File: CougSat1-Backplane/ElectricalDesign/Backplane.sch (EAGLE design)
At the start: 16 parts, among them J1 COUGSATBUSBACKPLANE, J2 COUGSATBUSBACKPLANE, J3 COUGSATBUSBACKPLANE, J4 COUGSATBUSBACKPLANE, J5 COUGSATBUSBACKPLANE, J6 COUGSATBUSBACKPLANE, J7 COUGSATBUSBACKPLANE, J8 COUGSATBUSBACKPLANE

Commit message: Updated Backplane Schematic
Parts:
- removed H3, H4: MOUNTING_HOLE_PLAIN3MMBOLT, CougsInSpace:MOUNTING_HOLE_PLAIN3MMBOLT
- removed IMG1: COUGSINSPACELOGOSMALL, CougsInSpace:COUGSINSPACELOGOSMALL
- removed IMG2: COUGSINSPACELOGOTEXT, CougsInSpace:COUGSINSPACELOGOTEXT
- removed IMG3: SIGNATUREHENDRIK, CougsInSpace:SIGNATUREHENDRIK
- removed IMG4: SIGNATUREHENDRIK-HAM, CougsInSpace:SIGNATUREHENDRIK-HAM
- added C1, C2: 100nF 10%, CougsInSpace-Capacitors:CAP-V-100NF-1608
- added J10, J9: Deployment Switch, CougsInSpace-Connectors:1X04-PICOLOCK
- added R1, R2: 0Ω <20mΩ, CougsInSpace-Resistors:RES-V-0-1608
- H1, H2: value MOUNTING_HOLE_PLAIN3MMBOLT -> M3; device CougsInSpace:MOUNTING_HOLE_PLAIN3MMBOLT -> CougsInSpace-Hardware:MOUNTING_HOLE-3.3
- J1, J2, J3, J4, J5, J6, J7, J8: value COUGSATBUSBACKPLANE -> CougSat Socket; device CougsInSpace:COUGSATBUSBACKPLANE -> CougsInSpace-Connectors:CIS_CARD-SODIMM-DDR1
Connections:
- removed net COM_IRQ: J1RCS.COM_IRQ, J2RCS.COM_IRQ, J3RCS.COM_IRQ, J4RCS.COM_IRQ, J5RCS.COM_IRQ, J6RCS.COM_IRQ, J7RCS.COM_IRQ, J8RCS.COM_IRQ
- removed net COM_USART_CLK: J1RCS.COM_USART_CLK, J2RCS.COM_USART_CLK, J3RCS.COM_USART_CLK, J4RCS.COM_USART_CLK, J5RCS.COM_USART_CLK, J6RCS.COM_USART_CLK, J7RCS.COM_USART_CLK, J8RCS.COM_USART_CLK
- removed net COM_USART_RX: J1RCS.COM_USART_RX, J2RCS.COM_USART_RX, J3RCS.COM_USART_RX, J4RCS.COM_USART_RX, J5RCS.COM_USART_RX, J6RCS.COM_USART_RX, J7RCS.COM_USART_RX, J8RCS.COM_USART_RX
- removed net COM_USART_TX: J1RCS.COM_USART_TX, J2RCS.COM_USART_TX, J3RCS.COM_USART_TX, J4RCS.COM_USART_TX, J5RCS.COM_USART_TX, J6RCS.COM_USART_TX, J7RCS.COM_USART_TX, J8RCS.COM_USART_TX
- removed net CTRL_RESET: J1DATABUS.CTRL_!RESET, J2DATABUS.CTRL_!RESET, J3DATABUS.CTRL_!RESET, J4DATABUS.CTRL_!RESET, J5DATABUS.CTRL_!RESET, J6DATABUS.CTRL_!RESET, J7DATABUS.CTRL_!RESET, J8DATABUS.CTRL_!RESET
- removed net GPIO_153: J1GPIO.GPIO_153, J2GPIO.GPIO_153, J3GPIO.GPIO_153, J4GPIO.GPIO_153, J5GPIO.GPIO_153, J6GPIO.GPIO_153, J7GPIO.GPIO_153, J8GPIO.GPIO_153
- removed net GPIO_155: J1GPIO.GPIO_155, J2GPIO.GPIO_155, J3GPIO.GPIO_155, J4GPIO.GPIO_155, J5GPIO.GPIO_155, J6GPIO.GPIO_155, J7GPIO.GPIO_155, J8GPIO.GPIO_155
- removed net GPIO_157: J1GPIO.GPIO_157, J2GPIO.GPIO_157, J3GPIO.GPIO_157, J4GPIO.GPIO_157, J5GPIO.GPIO_157, J6GPIO.GPIO_157, J7GPIO.GPIO_157, J8GPIO.GPIO_157
- removed net GPIO_158: J1GPIO.GPIO_158, J2GPIO.GPIO_158, J3GPIO.GPIO_158, J4GPIO.GPIO_158, J5GPIO.GPIO_158, J6GPIO.GPIO_158, J7GPIO.GPIO_158, J8GPIO.GPIO_158
- removed net GPIO_159: J1GPIO.GPIO_159, J2GPIO.GPIO_159, J3GPIO.GPIO_159, J4GPIO.GPIO_159, J5GPIO.GPIO_159, J6GPIO.GPIO_159, J7GPIO.GPIO_159, J8GPIO.GPIO_159
- removed net GPIO_161: J1GPIO.GPIO_161, J2GPIO.GPIO_161, J3GPIO.GPIO_161, J4GPIO.GPIO_161, J5GPIO.GPIO_161, J6GPIO.GPIO_161, J7GPIO.GPIO_161, J8GPIO.GPIO_161
- removed net GPIO_163: J1GPIO.GPIO_163, J2GPIO.GPIO_163, J3GPIO.GPIO_163, J4GPIO.GPIO_163, J5GPIO.GPIO_163, J6GPIO.GPIO_163, J7GPIO.GPIO_163, J8GPIO.GPIO_163
- removed net GPIO_165: J1GPIO.GPIO_165, J2GPIO.GPIO_165, J3GPIO.GPIO_165, J4GPIO.GPIO_165, J5GPIO.GPIO_165, J6GPIO.GPIO_165, J7GPIO.GPIO_165, J8GPIO.GPIO_165
- removed net GPIO_167: J1GPIO.GPIO_167, J2GPIO.GPIO_167, J3GPIO.GPIO_167, J4GPIO.GPIO_167, J5GPIO.GPIO_167, J6GPIO.GPIO_167, J7GPIO.GPIO_167, J8GPIO.GPIO_167
- removed net PMIC_I2C_SCL: J1DATABUS.PMIC_I2C_SCL, J2DATABUS.PMIC_I2C_SCL, J3DATABUS.PMIC_I2C_SCL, J4DATABUS.PMIC_I2C_SCL, J5DATABUS.PMIC_I2C_SCL, J6DATABUS.PMIC_I2C_SCL, J7DATABUS.PMIC_I2C_SCL, J8DATABUS.PMIC_I2C_SCL
- removed net PMIC_I2C_SDA: J1DATABUS.PMIC_I2C_SDA, J2DATABUS.PMIC_I2C_SDA, J3DATABUS.PMIC_I2C_SDA, J4DATABUS.PMIC_I2C_SDA, J5DATABUS.PMIC_I2C_SDA, J6DATABUS.PMIC_I2C_SDA, J7DATABUS.PMIC_I2C_SDA, J8DATABUS.PMIC_I2C_SDA
- removed net PWR_CTRL_UMB: J1POWER.PWR_CTRL_UMB, J2POWER.PWR_CTRL_UMB, J3POWER.PWR_CTRL_UMB, J4POWER.PWR_CTRL_UMB, J5POWER.PWR_CTRL_UMB, J6POWER.PWR_CTRL_UMB, J7POWER.PWR_CTRL_UMB, J8POWER.PWR_CTRL_UMB
- removed net SUP_3V3_0: J1POWER.SUP_3V3_0, J2POWER.SUP_3V3_0, J3POWER.SUP_3V3_0, J4POWER.SUP_3V3_0, J5POWER.SUP_3V3_0, J6POWER.SUP_3V3_0, J7POWER.SUP_3V3_0, J8POWER.SUP_3V3_0
- removed net SUP_3V3_1: J1POWER.SUP_3V3_1, J2POWER.SUP_3V3_1, J3POWER.SUP_3V3_1, J4POWER.SUP_3V3_1, J5POWER.SUP_3V3_1, J6POWER.SUP_3V3_1, J7POWER.SUP_3V3_1, J8POWER.SUP_3V3_1
- removed net SUP_3V3_2: J1POWER.SUP_3V3_2, J2POWER.SUP_3V3_2, J3POWER.SUP_3V3_2, J4POWER.SUP_3V3_2, J5POWER.SUP_3V3_2, J6POWER.SUP_3V3_2, J7POWER.SUP_3V3_2, J8POWER.SUP_3V3_2
- removed net SUP_3V3_3: J1POWER.SUP_3V3_3, J2POWER.SUP_3V3_3, J3POWER.SUP_3V3_3, J4POWER.SUP_3V3_3, J5POWER.SUP_3V3_3, J6POWER.SUP_3V3_3, J7POWER.SUP_3V3_3, J8POWER.SUP_3V3_3
- removed net SUP_3V3_4: J1POWER.SUP_3V3_4, J2POWER.SUP_3V3_4, J3POWER.SUP_3V3_4, J4POWER.SUP_3V3_4, J5POWER.SUP_3V3_4, J6POWER.SUP_3V3_4, J7POWER.SUP_3V3_4, J8POWER.SUP_3V3_4
- removed net SUP_3V3_5: J1POWER.SUP_3V3_5, J2POWER.SUP_3V3_5, J3POWER.SUP_3V3_5, J4POWER.SUP_3V3_5, J5POWER.SUP_3V3_5, J6POWER.SUP_3V3_5, J7POWER.SUP_3V3_5, J8POWER.SUP_3V3_5
- removed net SUP_5V0_0: J1POWER.SUP_5V0_0, J2POWER.SUP_5V0_0, J3POWER.SUP_5V0_0, J4POWER.SUP_5V0_0, J5POWER.SUP_5V0_0, J6POWER.SUP_5V0_0, J7POWER.SUP_5V0_0, J8POWER.SUP_5V0_0
- removed net SUP_5V0_1: J1POWER.SUP_5V0_1, J2POWER.SUP_5V0_1, J3POWER.SUP_5V0_1, J4POWER.SUP_5V0_1, J5POWER.SUP_5V0_1, J6POWER.SUP_5V0_1, J7POWER.SUP_5V0_1, J8POWER.SUP_5V0_1
- removed net SUP_5VIN: J1POWER.SUP_5VIN, J2POWER.SUP_5VIN, J3POWER.SUP_5VIN, J4POWER.SUP_5VIN, J5POWER.SUP_5VIN, J6POWER.SUP_5VIN, J7POWER.SUP_5VIN, J8POWER.SUP_5VIN
- removed net SUP_UNREG_0: J1POWER.SUP_UNREG_0, J2POWER.SUP_UNREG_0, J3POWER.SUP_UNREG_0, J4POWER.SUP_UNREG_0, J5POWER.SUP_UNREG_0, J6POWER.SUP_UNREG_0, J7POWER.SUP_UNREG_0, J8POWER.SUP_UNREG_0
- removed net SUP_UNREG_1: J1POWER.SUP_UNREG_1, J2POWER.SUP_UNREG_1, J3POWER.SUP_UNREG_1, J4POWER.SUP_UNREG_1, J5POWER.SUP_UNREG_1, J6POWER.SUP_UNREG_1, J7POWER.SUP_UNREG_1, J8POWER.SUP_UNREG_1
- new net BUS_JTAG_EN-0: J1JTAG.BUS_JTAG_EN-0, J2JTAG.BUS_JTAG_EN-0, J3JTAG.BUS_JTAG_EN-0, J4JTAG.BUS_JTAG_EN-0, J5JTAG.BUS_JTAG_EN-0, J6JTAG.BUS_JTAG_EN-0, J7JTAG.BUS_JTAG_EN-0, J8JTAG.BUS_JTAG_EN-0
- new net BUS_JTAG_EN-1: J1JTAG.BUS_JTAG_EN-1, J2JTAG.BUS_JTAG_EN-1, J3JTAG.BUS_JTAG_EN-1, J4JTAG.BUS_JTAG_EN-1, J5JTAG.BUS_JTAG_EN-1, J6JTAG.BUS_JTAG_EN-1, J7JTAG.BUS_JTAG_EN-1, J8JTAG.BUS_JTAG_EN-1
- new net BUS_JTAG_EN-2: J1JTAG.BUS_JTAG_EN-2, J2JTAG.BUS_JTAG_EN-2, J3JTAG.BUS_JTAG_EN-2, J4JTAG.BUS_JTAG_EN-2, J5JTAG.BUS_JTAG_EN-2, J6JTAG.BUS_JTAG_EN-2, J7JTAG.BUS_JTAG_EN-2, J8JTAG.BUS_JTAG_EN-2
- new net BUS_JTAG_EN-3: J1JTAG.BUS_JTAG_EN-3, J2JTAG.BUS_JTAG_EN-3, J3JTAG.BUS_JTAG_EN-3, J4JTAG.BUS_JTAG_EN-3, J5JTAG.BUS_JTAG_EN-3, J6JTAG.BUS_JTAG_EN-3, J7JTAG.BUS_JTAG_EN-3, J8JTAG.BUS_JTAG_EN-3
- new net CHASSIS: C1.1, C2.1, H1.MOUNT, H2.MOUNT, R1.2, R2.2
- new net COM_SPI_CS: J1DATA.COM_SPI_CS, J2DATA.COM_SPI_CS, J3DATA.COM_SPI_CS, J4DATA.COM_SPI_CS, J5DATA.COM_SPI_CS, J6DATA.COM_SPI_CS, J7DATA.COM_SPI_CS, J8DATA.COM_SPI_CS
- new net COM_SPI_MISO: J1DATA.COM_SPI_MISO, J2DATA.COM_SPI_MISO, J3DATA.COM_SPI_MISO, J4DATA.COM_SPI_MISO, J5DATA.COM_SPI_MISO, J6DATA.COM_SPI_MISO, J7DATA.COM_SPI_MISO, J8DATA.COM_SPI_MISO
- new net COM_SPI_MOSI: J1DATA.COM_SPI_MOSI, J2DATA.COM_SPI_MOSI, J3DATA.COM_SPI_MOSI, J4DATA.COM_SPI_MOSI, J5DATA.COM_SPI_MOSI, J6DATA.COM_SPI_MOSI, J7DATA.COM_SPI_MOSI, J8DATA.COM_SPI_MOSI
- new net COM_SPI_SCK: J1DATA.COM_SPI_SCK, J2DATA.COM_SPI_SCK, J3DATA.COM_SPI_SCK, J4DATA.COM_SPI_SCK, J5DATA.COM_SPI_SCK, J6DATA.COM_SPI_SCK, J7DATA.COM_SPI_SCK, J8DATA.COM_SPI_SCK
- new net CTRL_!RESET: J1DATA.CTRL_!RESET, J2DATA.CTRL_!RESET, J3DATA.CTRL_!RESET, J4DATA.CTRL_!RESET, J5DATA.CTRL_!RESET, J6DATA.CTRL_!RESET, J7DATA.CTRL_!RESET, J8DATA.CTRL_!RESET
- new net GPIO-0: J1GPIO.GPIO-0, J2GPIO.GPIO-0, J3GPIO.GPIO-0, J4GPIO.GPIO-0, J5GPIO.GPIO-0, J6GPIO.GPIO-0, J7GPIO.GPIO-0, J8GPIO.GPIO-0
- new net GPIO-1: J1GPIO.GPIO-1, J2GPIO.GPIO-1, J3GPIO.GPIO-1, J4GPIO.GPIO-1, J5GPIO.GPIO-1, J6GPIO.GPIO-1, J7GPIO.GPIO-1, J8GPIO.GPIO-1
- new net GPIO-2: J1GPIO.GPIO-2, J2GPIO.GPIO-2, J3GPIO.GPIO-2, J4GPIO.GPIO-2, J5GPIO.GPIO-2, J6GPIO.GPIO-2, J7GPIO.GPIO-2, J8GPIO.GPIO-2
- new net GPIO-3: J1GPIO.GPIO-3, J2GPIO.GPIO-3, J3GPIO.GPIO-3, J4GPIO.GPIO-3, J5GPIO.GPIO-3, J6GPIO.GPIO-3, J7GPIO.GPIO-3, J8GPIO.GPIO-3
- new net GPIO-4: J1GPIO.GPIO-4, J2GPIO.GPIO-4, J3GPIO.GPIO-4, J4GPIO.GPIO-4, J5GPIO.GPIO-4, J6GPIO.GPIO-4, J7GPIO.GPIO-4, J8GPIO.GPIO-4
- new net GPIO-5: J1GPIO.GPIO-5, J2GPIO.GPIO-5, J3GPIO.GPIO-5, J4GPIO.GPIO-5, J5GPIO.GPIO-5, J6GPIO.GPIO-5, J7GPIO.GPIO-5, J8GPIO.GPIO-5
- new net GPIO-6: J1GPIO.GPIO-6, J2GPIO.GPIO-6, J3GPIO.GPIO-6, J4GPIO.GPIO-6, J5GPIO.GPIO-6, J6GPIO.GPIO-6, J7GPIO.GPIO-6, J8GPIO.GPIO-6
- new net GPIO-7: J1GPIO.GPIO-7, J2GPIO.GPIO-7, J3GPIO.GPIO-7, J4GPIO.GPIO-7, J5GPIO.GPIO-7, J6GPIO.GPIO-7, J7GPIO.GPIO-7, J8GPIO.GPIO-7
- new net GPIO-8: J1GPIO.GPIO-8, J2GPIO.GPIO-8, J3GPIO.GPIO-8, J4GPIO.GPIO-8, J5GPIO.GPIO-8, J6GPIO.GPIO-8, J7GPIO.GPIO-8, J8GPIO.GPIO-8
- new net GPIO-9: J1GPIO.GPIO-9, J2GPIO.GPIO-9, J3GPIO.GPIO-9, J4GPIO.GPIO-9, J5GPIO.GPIO-9, J6GPIO.GPIO-9, J7GPIO.GPIO-9, J8GPIO.GPIO-9
- new net PR_3.3V-0: J1POWER.PR_3.3V-0, J2POWER.PR_3.3V-0, J3POWER.PR_3.3V-0, J4POWER.PR_3.3V-0, J5POWER.PR_3.3V-0, J6POWER.PR_3.3V-0, J7POWER.PR_3.3V-0, J8POWER.PR_3.3V-0
- new net PR_3.3V-1: J1POWER.PR_3.3V-1, J2POWER.PR_3.3V-1, J3POWER.PR_3.3V-1, J4POWER.PR_3.3V-1, J5POWER.PR_3.3V-1, J6POWER.PR_3.3V-1, J7POWER.PR_3.3V-1, J8POWER.PR_3.3V-1
- new net PR_3.3V-10: J1POWER.PR_3.3V-10, J2POWER.PR_3.3V-10, J3POWER.PR_3.3V-10, J4POWER.PR_3.3V-10, J5POWER.PR_3.3V-10, J6POWER.PR_3.3V-10, J7POWER.PR_3.3V-10, J8POWER.PR_3.3V-10
- new net PR_3.3V-11: J1POWER.PR_3.3V-11, J2POWER.PR_3.3V-11, J3POWER.PR_3.3V-11, J4POWER.PR_3.3V-11, J5POWER.PR_3.3V-11, J6POWER.PR_3.3V-11, J7POWER.PR_3.3V-11, J8POWER.PR_3.3V-11
- new net PR_3.3V-12: J1POWER.PR_3.3V-12, J2POWER.PR_3.3V-12, J3POWER.PR_3.3V-12, J4POWER.PR_3.3V-12, J5POWER.PR_3.3V-12, J6POWER.PR_3.3V-12, J7POWER.PR_3.3V-12, J8POWER.PR_3.3V-12
- new net PR_3.3V-2: J1POWER.PR_3.3V-2, J2POWER.PR_3.3V-2, J3POWER.PR_3.3V-2, J4POWER.PR_3.3V-2, J5POWER.PR_3.3V-2, J6POWER.PR_3.3V-2, J7POWER.PR_3.3V-2, J8POWER.PR_3.3V-2
- new net PR_3.3V-3: J1POWER.PR_3.3V-3, J2POWER.PR_3.3V-3, J3POWER.PR_3.3V-3, J4POWER.PR_3.3V-3, J5POWER.PR_3.3V-3, J6POWER.PR_3.3V-3, J7POWER.PR_3.3V-3, J8POWER.PR_3.3V-3
- new net PR_3.3V-4: J1POWER.PR_3.3V-4, J2POWER.PR_3.3V-4, J3POWER.PR_3.3V-4, J4POWER.PR_3.3V-4, J5POWER.PR_3.3V-4, J6POWER.PR_3.3V-4, J7POWER.PR_3.3V-4, J8POWER.PR_3.3V-4
- new net PR_3.3V-5: J1POWER.PR_3.3V-5, J2POWER.PR_3.3V-5, J3POWER.PR_3.3V-5, J4POWER.PR_3.3V-5, J5POWER.PR_3.3V-5, J6POWER.PR_3.3V-5, J7POWER.PR_3.3V-5, J8POWER.PR_3.3V-5
- new net PR_3.3V-6: J1POWER.PR_3.3V-6, J2POWER.PR_3.3V-6, J3POWER.PR_3.3V-6, J4POWER.PR_3.3V-6, J5POWER.PR_3.3V-6, J6POWER.PR_3.3V-6, J7POWER.PR_3.3V-6, J8POWER.PR_3.3V-6
- new net PR_3.3V-7: J1POWER.PR_3.3V-7, J2POWER.PR_3.3V-7, J3POWER.PR_3.3V-7, J4POWER.PR_3.3V-7, J5POWER.PR_3.3V-7, J6POWER.PR_3.3V-7, J7POWER.PR_3.3V-7, J8POWER.PR_3.3V-7
- new net PR_3.3V-8: J1POWER.PR_3.3V-8, J2POWER.PR_3.3V-8, J3POWER.PR_3.3V-8, J4POWER.PR_3.3V-8, J5POWER.PR_3.3V-8, J6POWER.PR_3.3V-8, J7POWER.PR_3.3V-8, J8POWER.PR_3.3V-8
- new net PR_3.3V-9: J1POWER.PR_3.3V-9, J2POWER.PR_3.3V-9, J3POWER.PR_3.3V-9, J4POWER.PR_3.3V-9, J5POWER.PR_3.3V-9, J6POWER.PR_3.3V-9, J7POWER.PR_3.3V-9, J8POWER.PR_3.3V-9
- new net PR_BATT-0: J1POWER.PR_BATT-0, J2POWER.PR_BATT-0, J3POWER.PR_BATT-0, J4POWER.PR_BATT-0, J5POWER.PR_BATT-0, J6POWER.PR_BATT-0, J7POWER.PR_BATT-0, J8POWER.PR_BATT-0
- new net PR_BATT-1: J1POWER.PR_BATT-1, J2POWER.PR_BATT-1, J3POWER.PR_BATT-1, J4POWER.PR_BATT-1, J5POWER.PR_BATT-1, J6POWER.PR_BATT-1, J7POWER.PR_BATT-1, J8POWER.PR_BATT-1
- new net PR_BATT-2: J1POWER.PR_BATT-2, J2POWER.PR_BATT-2, J3POWER.PR_BATT-2, J4POWER.PR_BATT-2, J5POWER.PR_BATT-2, J6POWER.PR_BATT-2, J7POWER.PR_BATT-2, J8POWER.PR_BATT-2
- new net PR_BATT-3: J1POWER.PR_BATT-3, J2POWER.PR_BATT-3, J3POWER.PR_BATT-3, J4POWER.PR_BATT-3, J5POWER.PR_BATT-3, J6POWER.PR_BATT-3, J7POWER.PR_BATT-3, J8POWER.PR_BATT-3
- new net PR_BATT-4: J1POWER.PR_BATT-4, J2POWER.PR_BATT-4, J3POWER.PR_BATT-4, J4POWER.PR_BATT-4, J5POWER.PR_BATT-4, J6POWER.PR_BATT-4, J7POWER.PR_BATT-4, J8POWER.PR_BATT-4
- new net PR_BATT-5: J1POWER.PR_BATT-5, J2POWER.PR_BATT-5, J3POWER.PR_BATT-5, J4POWER.PR_BATT-5, J5POWER.PR_BATT-5, J6POWER.PR_BATT-5, J7POWER.PR_BATT-5, J8POWER.PR_BATT-5
- new net PR_BATT-6: J1POWER.PR_BATT-6, J2POWER.PR_BATT-6, J3POWER.PR_BATT-6, J4POWER.PR_BATT-6, J5POWER.PR_BATT-6, J6POWER.PR_BATT-6, J7POWER.PR_BATT-6, J8POWER.PR_BATT-6
- net BUS_I2C0_IRQ: now also J1DATA.BUS_I2C0_IRQ, J2DATA.BUS_I2C0_IRQ, J3DATA.BUS_I2C0_IRQ, J4DATA.BUS_I2C0_IRQ, J5DATA.BUS_I2C0_IRQ, J6DATA.BUS_I2C0_IRQ, J7DATA.BUS_I2C0_IRQ, J8DATA.BUS_I2C0_IRQ; no longer J1DATABUS.BUS_I2C0_IRQ, J2DATABUS.BUS_I2C0_IRQ, J3DATABUS.BUS_I2C0_IRQ, J4DATABUS.BUS_I2C0_IRQ, J5DATABUS.BUS_I2C0_IRQ, J6DATABUS.BUS_I2C0_IRQ, J7DATABUS.BUS_I2C0_IRQ, J8DATABUS.BUS_I2C0_IRQ
- net BUS_I2C0_SCL: now also J1DATA.BUS_I2C0_SCL, J2DATA.BUS_I2C0_SCL, J3DATA.BUS_I2C0_SCL, J4DATA.BUS_I2C0_SCL, J5DATA.BUS_I2C0_SCL, J6DATA.BUS_I2C0_SCL, J7DATA.BUS_I2C0_SCL, J8DATA.BUS_I2C0_SCL; no longer J1DATABUS.BUS_I2C0_SCL, J2DATABUS.BUS_I2C0_SCL, J3DATABUS.BUS_I2C0_SCL, J4DATABUS.BUS_I2C0_SCL, J5DATABUS.BUS_I2C0_SCL, J6DATABUS.BUS_I2C0_SCL, J7DATABUS.BUS_I2C0_SCL, J8DATABUS.BUS_I2C0_SCL
- net BUS_I2C0_SDA: now also J1DATA.BUS_I2C0_SDA, J2DATA.BUS_I2C0_SDA, J3DATA.BUS_I2C0_SDA, J4DATA.BUS_I2C0_SDA, J5DATA.BUS_I2C0_SDA, J6DATA.BUS_I2C0_SDA, J7DATA.BUS_I2C0_SDA, J8DATA.BUS_I2C0_SDA; no longer J1DATABUS.BUS_I2C0_SDA, J2DATABUS.BUS_I2C0_SDA, J3DATABUS.BUS_I2C0_SDA, J4DATABUS.BUS_I2C0_SDA, J5DATABUS.BUS_I2C0_SDA, J6DATABUS.BUS_I2C0_SDA, J7DATABUS.BUS_I2C0_SDA, J8DATABUS.BUS_I2C0_SDA
- net BUS_I2C1_IRQ: now also J1DATA.BUS_I2C1_IRQ, J2DATA.BUS_I2C1_IRQ, J3DATA.BUS_I2C1_IRQ, J4DATA.BUS_I2C1_IRQ, J5DATA.BUS_I2C1_IRQ, J6DATA.BUS_I2C1_IRQ, J7DATA.BUS_I2C1_IRQ, J8DATA.BUS_I2C1_IRQ; no longer J1DATABUS.BUS_I2C1_IRQ, J2DATABUS.BUS_I2C1_IRQ, J3DATABUS.BUS_I2C1_IRQ, J4DATABUS.BUS_I2C1_IRQ, J5DATABUS.BUS_I2C1_IRQ, J6DATABUS.BUS_I2C1_IRQ, J7DATABUS.BUS_I2C1_IRQ, J8DATABUS.BUS_I2C1_IRQ
- net BUS_I2C1_SCL: now also J1DATA.BUS_I2C1_SCL, J2DATA.BUS_I2C1_SCL, J3DATA.BUS_I2C1_SCL, J4DATA.BUS_I2C1_SCL, J5DATA.BUS_I2C1_SCL, J6DATA.BUS_I2C1_SCL, J7DATA.BUS_I2C1_SCL, J8DATA.BUS_I2C1_SCL; no longer J1DATABUS.BUS_I2C1_SCL, J2DATABUS.BUS_I2C1_SCL, J3DATABUS.BUS_I2C1_SCL, J4DATABUS.BUS_I2C1_SCL, J5DATABUS.BUS_I2C1_SCL, J6DATABUS.BUS_I2C1_SCL, J7DATABUS.BUS_I2C1_SCL, J8DATABUS.BUS_I2C1_SCL
- net BUS_I2C1_SDA: now also J1DATA.BUS_I2C1_SDA, J2DATA.BUS_I2C1_SDA, J3DATA.BUS_I2C1_SDA, J4DATA.BUS_I2C1_SDA, J5DATA.BUS_I2C1_SDA, J6DATA.BUS_I2C1_SDA, J7DATA.BUS_I2C1_SDA, J8DATA.BUS_I2C1_SDA; no longer J1DATABUS.BUS_I2C1_SDA, J2DATABUS.BUS_I2C1_SDA, J3DATABUS.BUS_I2C1_SDA, J4DATABUS.BUS_I2C1_SDA, J5DATABUS.BUS_I2C1_SDA, J6DATABUS.BUS_I2C1_SDA, J7DATABUS.BUS_I2C1_SDA, J8DATABUS.BUS_I2C1_SDA
- net BUS_JTAG_TCK: now also J1JTAG.BUS_JTAG_TCK, J2JTAG.BUS_JTAG_TCK, J3JTAG.BUS_JTAG_TCK, J4JTAG.BUS_JTAG_TCK, J5JTAG.BUS_JTAG_TCK, J6JTAG.BUS_JTAG_TCK, J7JTAG.BUS_JTAG_TCK, J8JTAG.BUS_JTAG_TCK; no longer J1DATABUS.BUS_JTAG_TCK, J2DATABUS.BUS_JTAG_TCK, J3DATABUS.BUS_JTAG_TCK, J4DATABUS.BUS_JTAG_TCK, J5DATABUS.BUS_JTAG_TCK, J6DATABUS.BUS_JTAG_TCK, J7DATABUS.BUS_JTAG_TCK, J8DATABUS.BUS_JTAG_TCK
- net BUS_JTAG_TDI: now also J1JTAG.BUS_JTAG_TDI, J2JTAG.BUS_JTAG_TDI, J3JTAG.BUS_JTAG_TDI, J4JTAG.BUS_JTAG_TDI, J5JTAG.BUS_JTAG_TDI, J6JTAG.BUS_JTAG_TDI, J7JTAG.BUS_JTAG_TDI, J8JTAG.BUS_JTAG_TDI; no longer J1DATABUS.BUS_JTAG_TDI, J2DATABUS.BUS_JTAG_TDI, J3DATABUS.BUS_JTAG_TDI, J4DATABUS.BUS_JTAG_TDI, J5DATABUS.BUS_JTAG_TDI, J6DATABUS.BUS_JTAG_TDI, J7DATABUS.BUS_JTAG_TDI, J8DATABUS.BUS_JTAG_TDI
- net BUS_JTAG_TDO: now also J1JTAG.BUS_JTAG_TDO, J2JTAG.BUS_JTAG_TDO, J3JTAG.BUS_JTAG_TDO, J4JTAG.BUS_JTAG_TDO, J5JTAG.BUS_JTAG_TDO, J6JTAG.BUS_JTAG_TDO, J7JTAG.BUS_JTAG_TDO, J8JTAG.BUS_JTAG_TDO; no longer J1DATABUS.BUS_JTAG_TDO, J2DATABUS.BUS_JTAG_TDO, J3DATABUS.BUS_JTAG_TDO, J4DATABUS.BUS_JTAG_TDO, J5DATABUS.BUS_JTAG_TDO, J6DATABUS.BUS_JTAG_TDO, J7DATABUS.BUS_JTAG_TDO, J8DATABUS.BUS_JTAG_TDO
- net BUS_JTAG_TMS: now also J1JTAG.BUS_JTAG_TMS, J2JTAG.BUS_JTAG_TMS, J3JTAG.BUS_JTAG_TMS, J4JTAG.BUS_JTAG_TMS, J5JTAG.BUS_JTAG_TMS, J6JTAG.BUS_JTAG_TMS, J7JTAG.BUS_JTAG_TMS, J8JTAG.BUS_JTAG_TMS; no longer J1DATABUS.BUS_JTAG_TMS, J2DATABUS.BUS_JTAG_TMS, J3DATABUS.BUS_JTAG_TMS, J4DATABUS.BUS_JTAG_TMS, J5DATABUS.BUS_JTAG_TMS, J6DATABUS.BUS_JTAG_TMS, J7DATABUS.BUS_JTAG_TMS, J8DATABUS.BUS_JTAG_TMS
- net BUS_SPI_MISO: now also J1DATA.BUS_SPI_MISO, J2DATA.BUS_SPI_MISO, J3DATA.BUS_SPI_MISO, J4DATA.BUS_SPI_MISO, J5DATA.BUS_SPI_MISO, J6DATA.BUS_SPI_MISO, J7DATA.BUS_SPI_MISO, J8DATA.BUS_SPI_MISO; no longer J1DATABUS.BUS_SPI_MISO, J2DATABUS.BUS_SPI_MISO, J3DATABUS.BUS_SPI_MISO, J4DATABUS.BUS_SPI_MISO, J5DATABUS.BUS_SPI_MISO, J6DATABUS.BUS_SPI_MISO, J7DATABUS.BUS_SPI_MISO, J8DATABUS.BUS_SPI_MISO
- net BUS_SPI_MOSI: now also J1DATA.BUS_SPI_MOSI, J2DATA.BUS_SPI_MOSI, J3DATA.BUS_SPI_MOSI, J4DATA.BUS_SPI_MOSI, J5DATA.BUS_SPI_MOSI, J6DATA.BUS_SPI_MOSI, J7DATA.BUS_SPI_MOSI, J8DATA.BUS_SPI_MOSI; no longer J1DATABUS.BUS_SPI_MOSI, J2DATABUS.BUS_SPI_MOSI, J3DATABUS.BUS_SPI_MOSI, J4DATABUS.BUS_SPI_MOSI, J5DATABUS.BUS_SPI_MOSI, J6DATABUS.BUS_SPI_MOSI, J7DATABUS.BUS_SPI_MOSI, J8DATABUS.BUS_SPI_MOSI
- net BUS_SPI_SCK: now also J1DATA.BUS_SPI_SCK, J2DATA.BUS_SPI_SCK, J3DATA.BUS_SPI_SCK, J4DATA.BUS_SPI_SCK, J5DATA.BUS_SPI_SCK, J6DATA.BUS_SPI_SCK, J7DATA.BUS_SPI_SCK, J8DATA.BUS_SPI_SCK; no longer J1DATABUS.BUS_SPI_SCK, J2DATABUS.BUS_SPI_SCK, J3DATABUS.BUS_SPI_SCK, J4DATABUS.BUS_SPI_SCK, J5DATABUS.BUS_SPI_SCK, J6DATABUS.BUS_SPI_SCK, J7DATABUS.BUS_SPI_SCK, J8DATABUS.BUS_SPI_SCK
- net CTRL_SYNC: now also J1DATA.CTRL_SYNC, J2DATA.CTRL_SYNC, J3DATA.CTRL_SYNC, J4DATA.CTRL_SYNC, J5DATA.CTRL_SYNC, J6DATA.CTRL_SYNC, J7DATA.CTRL_SYNC, J8DATA.CTRL_SYNC; no longer J1DATABUS.CTRL_SYNC, J2DATABUS.CTRL_SYNC, J3DATABUS.CTRL_SYNC, J4DATABUS.CTRL_SYNC, J5DATABUS.CTRL_SYNC, J6DATABUS.CTRL_SYNC, J7DATABUS.CTRL_SYNC, J8DATABUS.CTRL_SYNC
- net PGND: now also C1.2, C2.2, J10.3, J10.4, J1POWER.PGND, J2POWER.PGND, J3POWER.PGND, J4POWER.PGND, J5POWER.PGND, J6POWER.PGND, J7POWER.PGND, J8POWER.PGND, J9.3, J9.4, R1.1, R2.1; no longer J1POWER.PGND@1, J1POWER.PGND@2, J1POWER.PGND@3, J1POWER.PGND@4, J2POWER.PGND@1, J2POWER.PGND@2, J2POWER.PGND@3, J2POWER.PGND@4, J3POWER.PGND@1, J3POWER.PGND@2, J3POWER.PGND@3, J3POWER.PGND@4, J4POWER.PGND@1, J4POWER.PGND@2, J4POWER.PGND@3, J4POWER.PGND@4, J5POWER.PGND@1, J5POWER.PGND@2, J5POWER.PGND@3, J5POWER.PGND@4, J6POWER.PGND@1, J6POWER.PGND@2, J6POWER.PGND@3, J6POWER.PGND@4, J7POWER.PGND@1, J7POWER.PGND@2, J7POWER.PGND@3, J7POWER.PGND@4, J8POWER.PGND@1, J8POWER.PGND@2, J8POWER.PGND@3, J8POWER.PGND@4
- net PWR_CTRL_SW: now also J10.1, J10.2, J9.1, J9.2
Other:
- note added: "<2A6>"
- note added: "<2B6>"
- note added: "<2C6>"
- note added: "<3A6>"
- note added: "<3B6>"
- note added: "<3C6>"
- note added: "CAD Note: Mounting Holes"
- note added: "Connector: Deployment Switch"
- note added: "Page 1: Block Diagram Page 2: Data Bus Slots 0 - 3 Page 3: Data Bus Slots 4 - 7 Page 4: Power Bus Page 5: Mechanical"
- note added: "Page 2, 4"
- note added: "Page 3, 4"
- note added: "Page 4"
- note added: "Slot 0"
- note added: "Slot 1"
- note added: "Slot 2"
- note added: "Slot 3"
- note added: "Slot 4"
- note added: "Slot 5"
- note added: "Slot 6"
- note added: "Slot 7"
- note added: "Z"

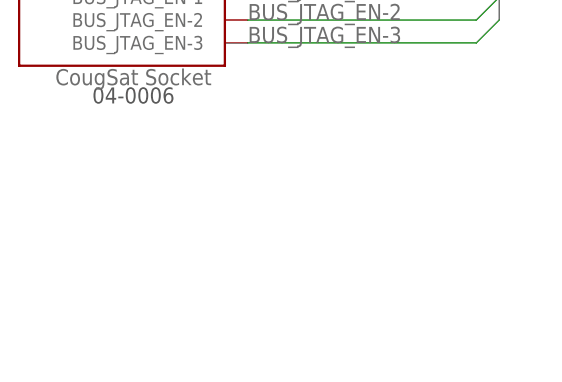
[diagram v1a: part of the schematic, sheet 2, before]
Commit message: Wrote Backplane Design Document
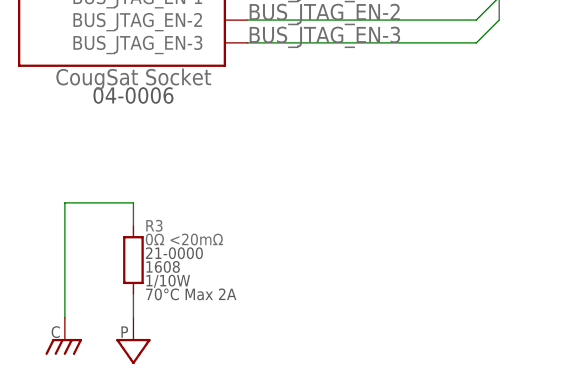
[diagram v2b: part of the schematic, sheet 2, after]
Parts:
- added R3: 0Ω <20mΩ, CougsInSpace-Resistors:RES-V-0-1608
- J10, J9: value Deployment Switch -> Separation Switch
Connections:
- net CHASSIS: now also R3.2
- net PGND: now also R3.1
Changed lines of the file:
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@@
 <part name="SUPPLY7" library="CougsInSpace-PowerSymbols" deviceset="PGND" device=""/>
 <part name="SUPPLY8" library="CougsInSpace-PowerSymbols" deviceset="PGND" device=""/>
-<part name="J9" library="CougsInSpace-Connectors" deviceset="1X04" device="-PICOLOCK" value="Deployment Switch"/>
+<part name="J9" library="CougsInSpace-Connectors" deviceset="1X04" device="-PICOLOCK" value="Separation Switch"/>
 <part name="SUPPLY9" library="CougsInSpace-PowerSymbols" deviceset="PGND" device=""/>
-<part name="J10" library="CougsInSpace-Connectors" deviceset="1X04" device="-PICOLOCK" value="Deployment Switch"/>
+<part name="J10" library="CougsInSpace-Connectors" deviceset="1X04" device="-PICOLOCK" value="Separation Switch"/>
 <part name="SUPPLY10" library="CougsInSpace-PowerSymbols" deviceset="PGND" device=""/>
 <part name="FRAME5" library="CougsInSpace-Aesthetics" deviceset="FRAME-A" device="">
@@
 <part name="C2" library="CougsInSpace-Capacitors" deviceset="CAP-V" device="-1608" technology="-100NF" value="100nF 10%"/>
 <part name="R2" library="CougsInSpace-Resistors" deviceset="RES-V" device="-1608" technology="-0" value="0Ω &lt;20mΩ"/>
+<part name="SUPPLY17" library="CougsInSpace-PowerSymbols" deviceset="PGND" device=""/>
+<part name="R3" library="CougsInSpace-Resistors" deviceset="RES-V" device="-1608" technology="-0" value="0Ω &lt;20mΩ"/>
+<part name="SUPPLY18" library="CougsInSpace-PowerSymbols" deviceset="CHASSIS" device=""/>
 </parts>
 <sheets>
@@
 <instance part="OFFSHEET2" gate="G$1" x="248.92" y="114.3"/>
 <instance part="OFFSHEET3" gate="G$1" x="248.92" y="71.12"/>
+<instance part="SUPPLY17" gate="G$1" x="17.78" y="12.7"/>
+<instance part="R3" gate="G$1" x="17.78" y="20.32"/>
+<instance part="SUPPLY18" gate="G$1" x="10.16" y="12.7"/>
 </instances>
 <busses>
@@
 </segment>
 </net>
+<net name="PGND" class="0">
+<segment>
+<pinref part="SUPPLY17" gate="G$1" pin="PGND"/>
+<pinref part="R3" gate="G$1" pin="1"/>
+<wire x1="17.78" y1="15.24" x2="17.78" y2="17.78" width="0.1524" layer="91"/>
+</segment>
+</net>
+<net name="CHASSIS" class="0">
+<segment>
+<pinref part="R3" gate="G$1" pin="2"/>
+<wire x1="17.78" y1="25.4" x2="17.78" y2="27.94" width="0.1524" layer="91"/>
+<pinref part="SUPPLY18" gate="G$1" pin="CHASSIS"/>
+<wire x1="17.78" y1="27.94" x2="10.16" y2="27.94" width="0.1524" layer="91"/>
+<wire x1="10.16" y1="27.94" x2="10.16" y2="15.24" width="0.1524" layer="91"/>
+</segment>
+</net>

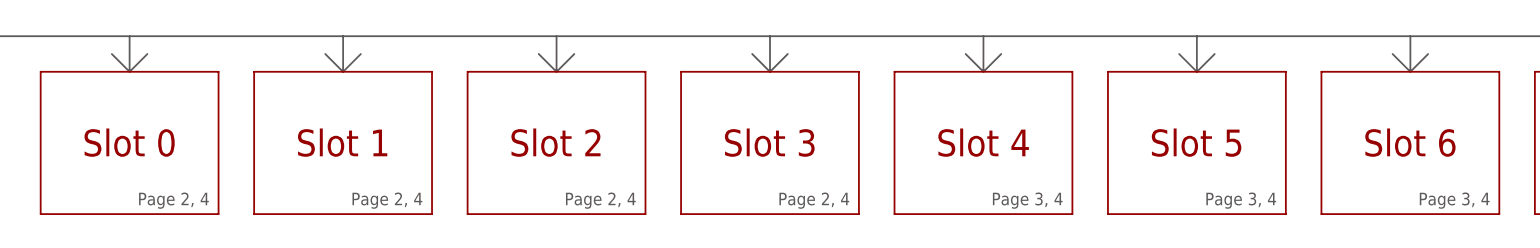
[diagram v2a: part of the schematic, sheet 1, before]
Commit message: Added Label to Block Diagram Connector
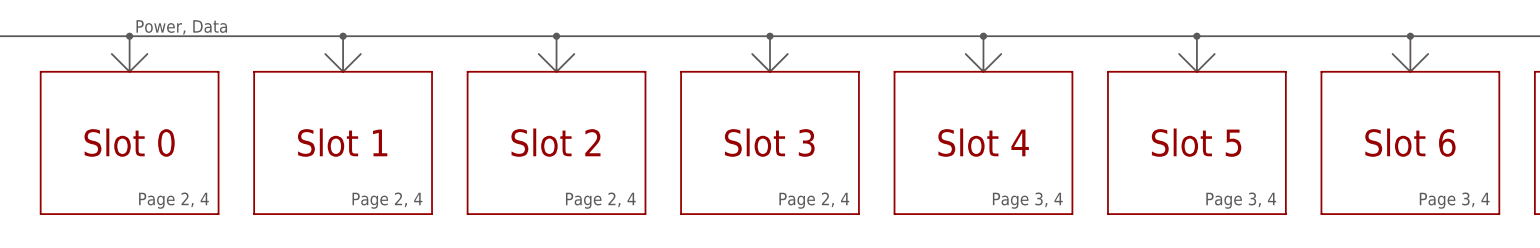
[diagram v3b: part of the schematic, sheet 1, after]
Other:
- note added: "Power, Data"
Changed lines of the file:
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@@
 <attribute name="PART_NUMBER" value="68-0005"/>
 <attribute name="PROJECT" value="CougSat-1: Backplane"/>
-<attribute name="REV" value="2.1.0"/>
+<attribute name="REV" value="2.1.1"/>
 </attributes>
 <variantdefs>
@@
 <part name="R3" library="CougsInSpace-Resistors" deviceset="RES-V" device="-1608" technology="-0" value="0Ω &lt;20mΩ"/>
 <part name="SUPPLY18" library="CougsInSpace-PowerSymbols" deviceset="CHASSIS" device=""/>
+<part name="DIA1" library="CougsInSpace-Aesthetics" deviceset="DIAGRAM-CONNECT_DOT" device=""/>
+<part name="DIA2" library="CougsInSpace-Aesthetics" deviceset="DIAGRAM-CONNECT_DOT" device=""/>
+<part name="DIA3" library="CougsInSpace-Aesthetics" deviceset="DIAGRAM-CONNECT_DOT" device=""/>
+<part name="DIA4" library="CougsInSpace-Aesthetics" deviceset="DIAGRAM-CONNECT_DOT" device=""/>
+<part name="DIA5" library="CougsInSpace-Aesthetics" deviceset="DIAGRAM-CONNECT_DOT" device=""/>
+<part name="DIA6" library="CougsInSpace-Aesthetics" deviceset="DIAGRAM-CONNECT_DOT" device=""/>
+<part name="DIA7" library="CougsInSpace-Aesthetics" deviceset="DIAGRAM-CONNECT_DOT" device=""/>
 </parts>
 <sheets>
@@
 <text x="222.25" y="102.87" size="1.778" layer="97" align="bottom-right">Page 3, 4</text>
 <text x="252.73" y="102.87" size="1.778" layer="97" align="bottom-right">Page 3, 4</text>
+<text x="28.702" y="127.508" size="1.778" layer="97">Power, Data</text>
 </plain>
 <instances>
@@
 <attribute name="TITLE" x="0" y="0" size="1.778" layer="96" display="off"/>
 </instance>
+<instance part="DIA1" gate="G$1" x="27.94" y="127"/>
+<instance part="DIA2" gate="G$1" x="58.42" y="127"/>
+<instance part="DIA3" gate="G$1" x="88.9" y="127"/>
+<instance part="DIA4" gate="G$1" x="119.38" y="127"/>
+<instance part="DIA5" gate="G$1" x="149.86" y="127"/>
+<instance part="DIA6" gate="G$1" x="180.34" y="127"/>
+<instance part="DIA7" gate="G$1" x="210.82" y="127"/>
 </instances>
 <busses>

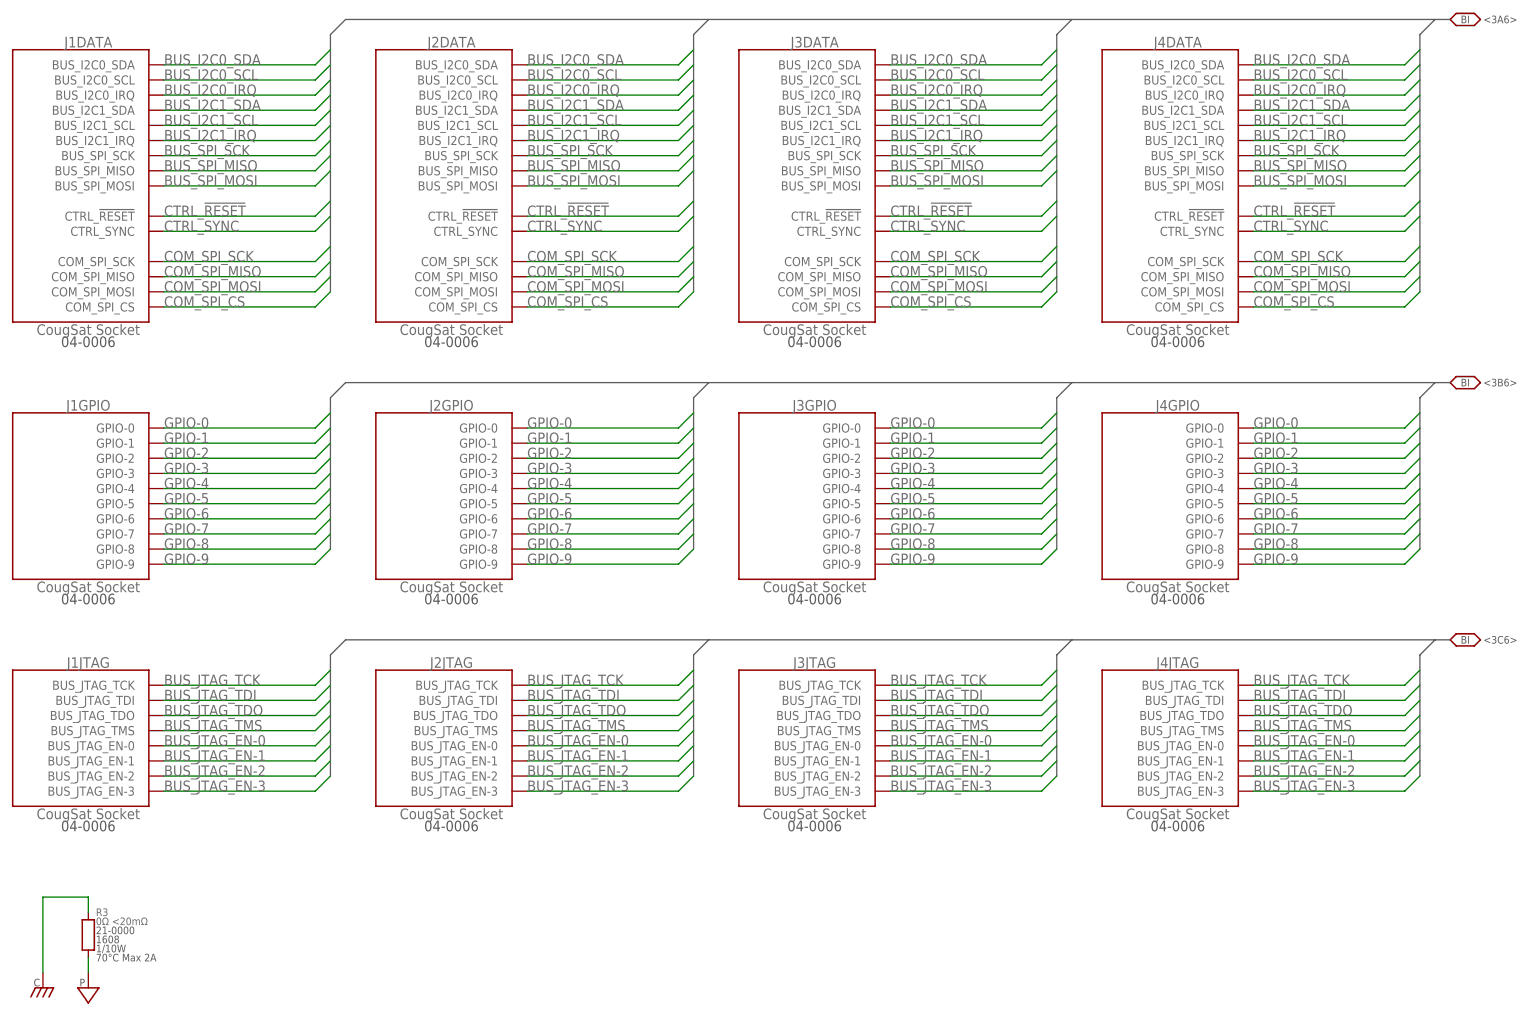
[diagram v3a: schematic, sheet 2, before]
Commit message: Laid Out Backplane
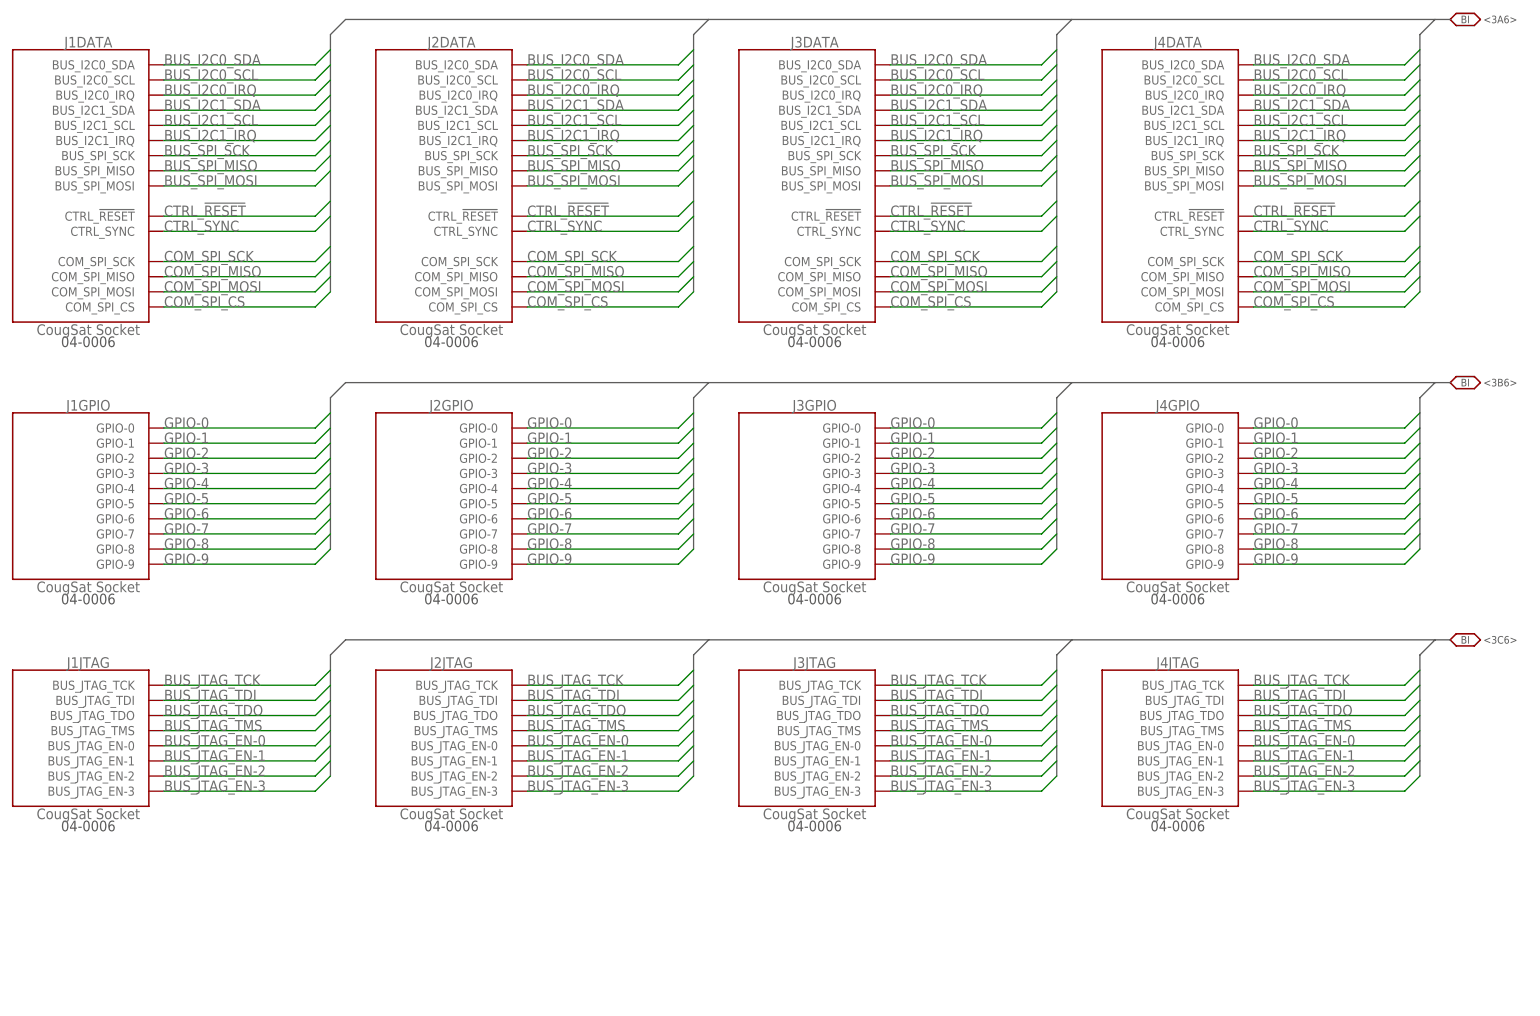
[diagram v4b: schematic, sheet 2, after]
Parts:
- removed R3: 0Ω <20mΩ, CougsInSpace-Resistors:RES-V-0-1608
- added LOGO1: SIGNATUREBRADLEY, CougsInSpace-Aesthetics:SIGNATUREBRADLEY
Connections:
- net CHASSIS: no longer R3.2
- net PGND: no longer R3.1
